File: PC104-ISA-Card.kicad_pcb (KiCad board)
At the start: 2 copper layers, 156.2 x 121.9 mm, 4 parts, among them J1 Bus_PC104_16bit, J2 Bus_ISA_16bit

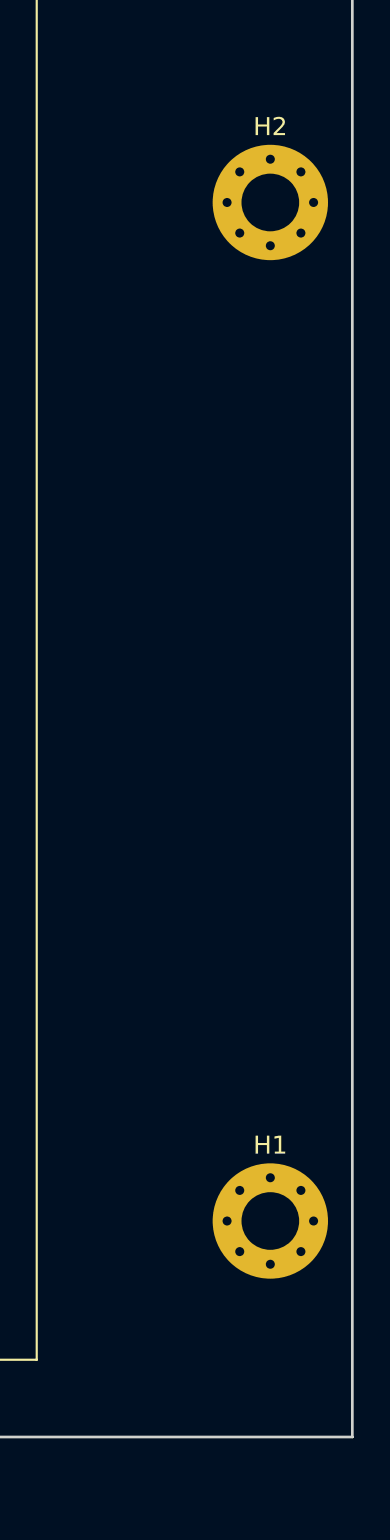
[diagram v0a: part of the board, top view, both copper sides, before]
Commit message: Move mounting holes to correct place for Keystone 9202
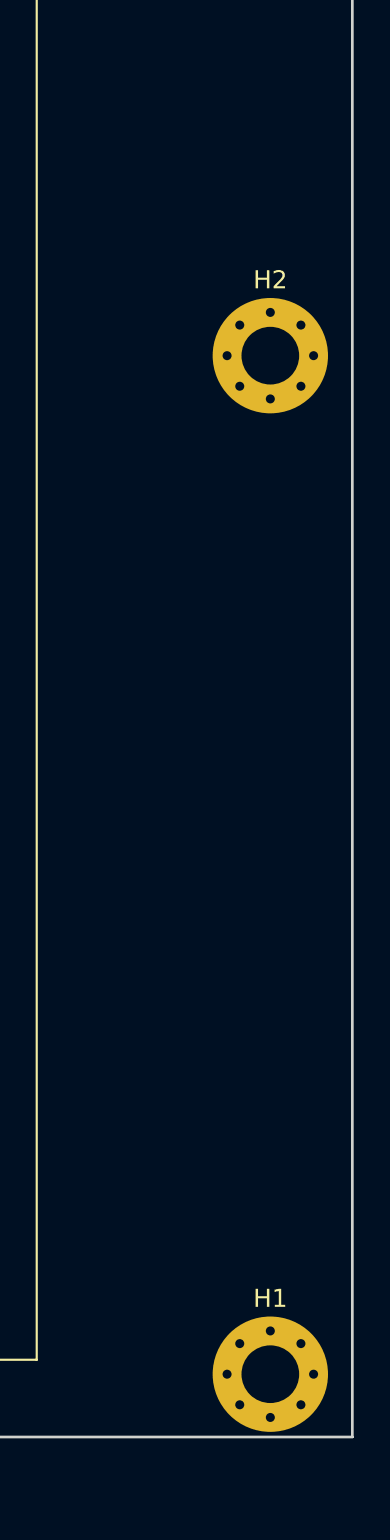
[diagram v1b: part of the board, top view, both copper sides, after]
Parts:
- moved H1 8.50 mm to (195.1, 149.0)
- moved H2 8.50 mm to (195.1, 92.5)
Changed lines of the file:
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@@
   (net 96 "unconnected-(J1-PadC19)")
   (footprint "MountingHole:MountingHole_3.2mm_M3_Pad_Via" (layer "F.Cu")
-    (at 195.08 140.515)
+    (at 195.08 149.015)
     (descr "Mounting Hole 3.2mm, M3")
     (tags "mounting hole 3.2mm m3")
@@
   )
   (footprint "MountingHole:MountingHole_3.2mm_M3_Pad_Via" (layer "F.Cu")
-    (at 195.08 84)
+    (at 195.08 92.5)
     (descr "Mounting Hole 3.2mm, M3")
     (tags "mounting hole 3.2mm m3")

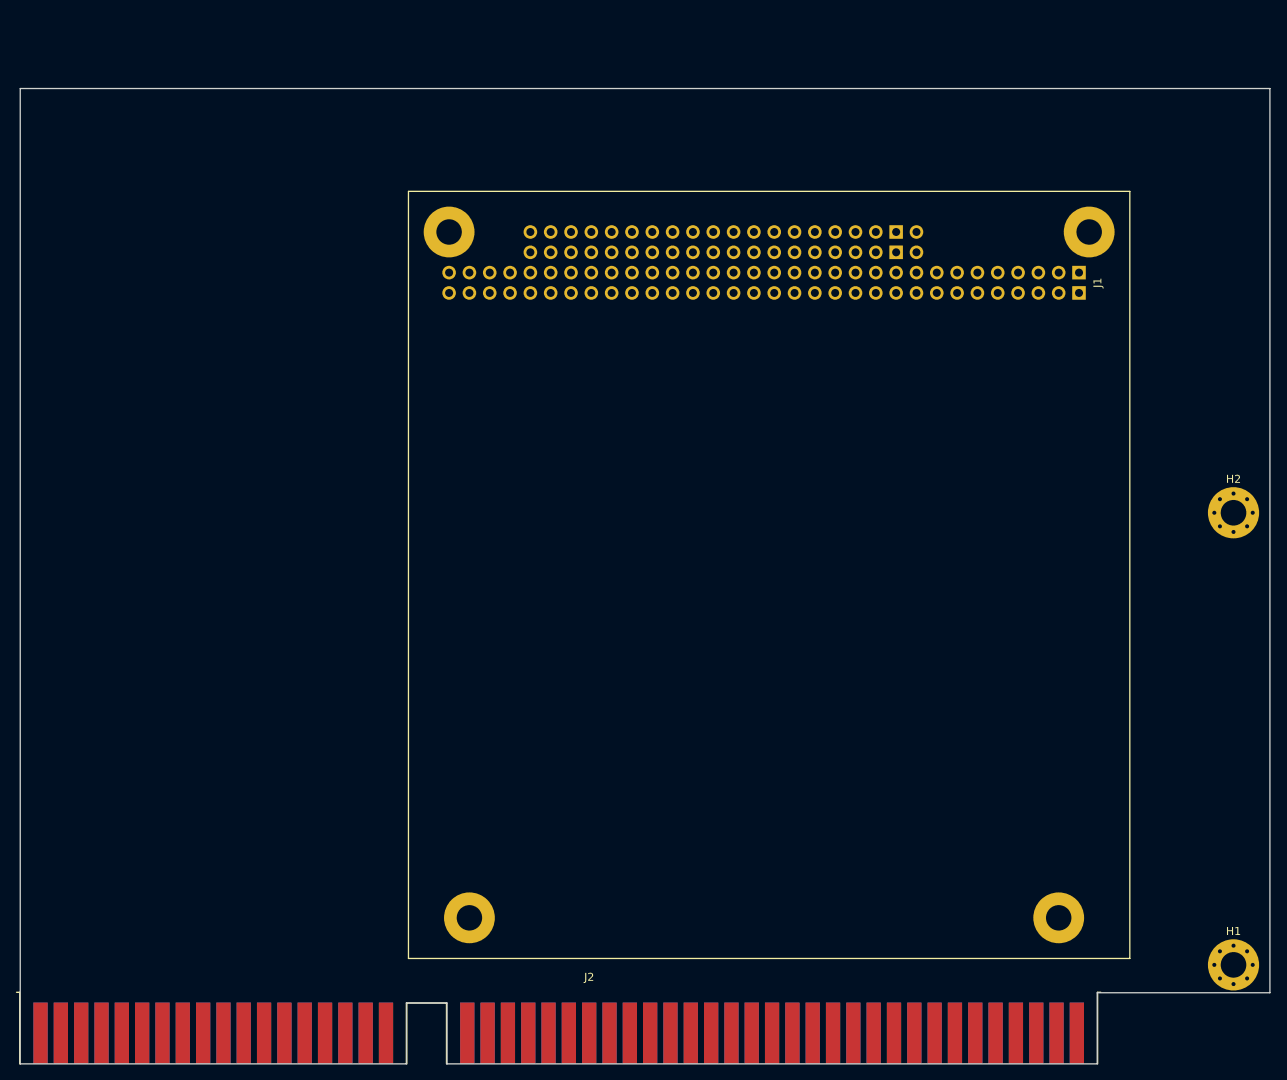
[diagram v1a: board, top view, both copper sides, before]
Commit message: Reduce board height
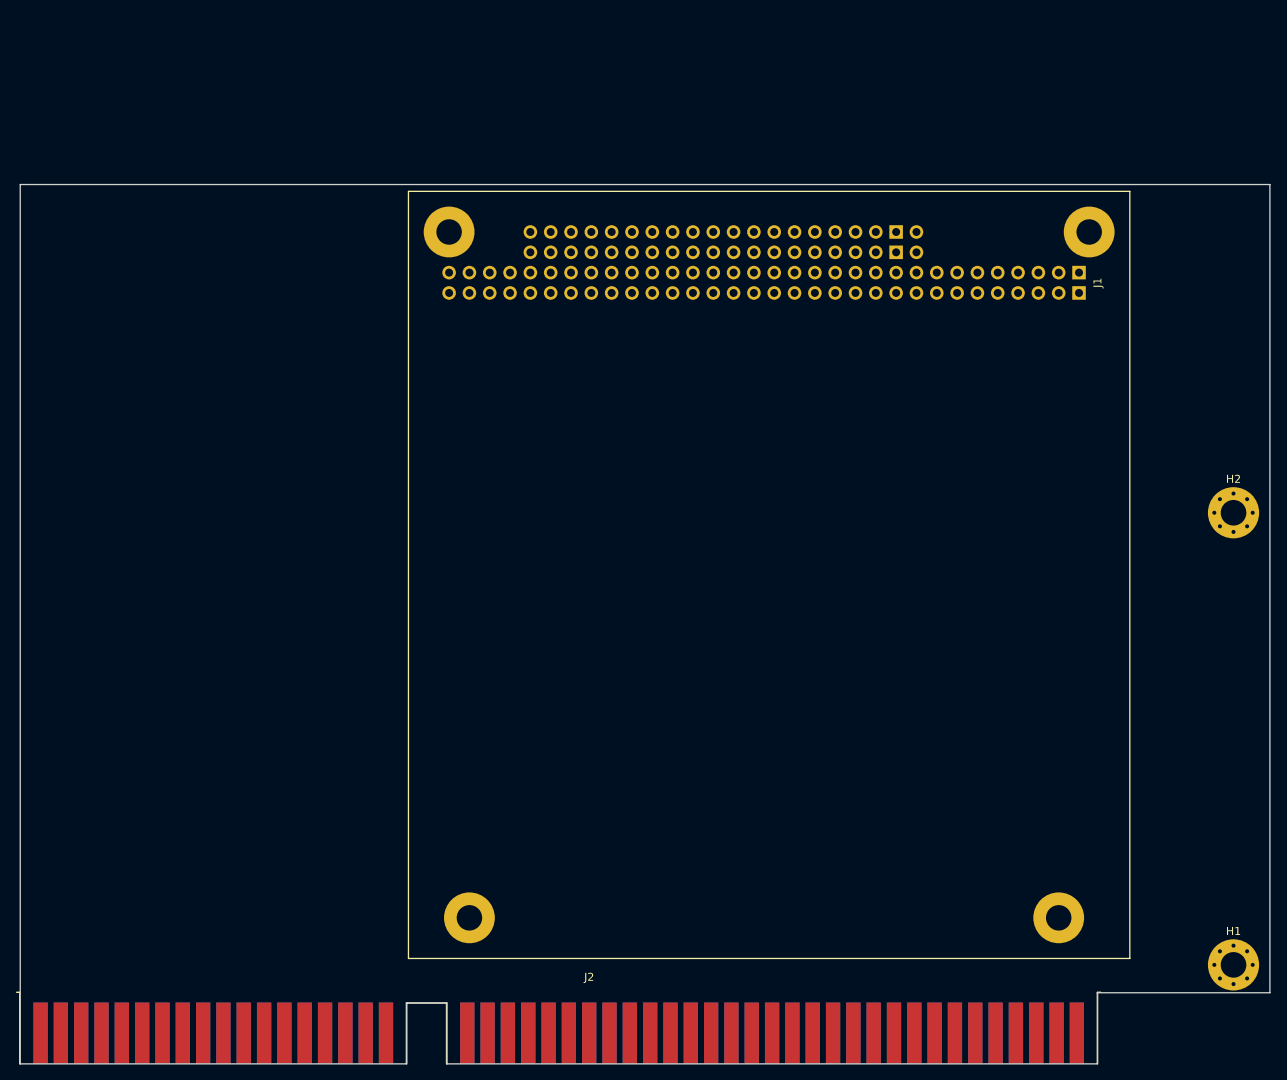
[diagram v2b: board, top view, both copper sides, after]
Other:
- board size 156.2 x 121.9 mm -> 156.2 x 109.9 mm
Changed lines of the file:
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@@
   (gr_line (start 43.42 161.39) (end 91.68 161.39) (layer "Edge.Cuts") (width 0.15))
   (gr_line (start 96.76 161.39) (end 178.04 161.39) (layer "Edge.Cuts") (width 0.15))
-  (gr_line (start 43.42 39.47) (end 43.42 161.39) (layer "Edge.Cuts") (width 0.15))
-  (gr_line (start 199.63 152.5) (end 199.63 39.47) (layer "Edge.Cuts") (width 0.15))
-  (gr_line (start 199.63 39.47) (end 43.42 39.47) (layer "Edge.Cuts") (width 0.15))
+  (gr_line (start 43.42 51.47) (end 43.42 161.39) (layer "Edge.Cuts") (width 0.15))
+  (gr_line (start 199.63 152.5) (end 199.63 51.47) (layer "Edge.Cuts") (width 0.15))
+  (gr_line (start 199.63 51.47) (end 43.42 51.47) (layer "Edge.Cuts") (width 0.15))
   (gr_line (start 96.76 153.77) (end 96.76 161.39) (layer "Edge.Cuts") (width 0.15))
   (gr_line (start 178.04 161.39) (end 178.04 152.5) (layer "Edge.Cuts") (width 0.15))

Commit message: Layout WIP
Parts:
- added C1: 10u, Capacitor_Tantalum_SMD:CP_EIA-7343-15_Kemet-W, F.Cu at (173.0, 71.8)
- added C2: 100n, Capacitor_SMD:C_0603_1608Metric, F.Cu at (65.5, 83.9)
- added C3: 10u, Capacitor_Tantalum_SMD:CP_EIA-7343-15_Kemet-W, F.Cu at (58.7, 91.5)
- added C4: 100n, Capacitor_SMD:C_0603_1608Metric, F.Cu at (61.2, 78.8)
- added C5: 10u, Capacitor_Tantalum_SMD:CP_EIA-7343-15_Kemet-W, F.Cu at (65.4, 101.9)
- added C6: 100n, Capacitor_SMD:C_0603_1608Metric, F.Cu at (70.7, 78.2)
- added C7: 10u, Capacitor_Tantalum_SMD:CP_EIA-7343-15_Kemet-W, F.Cu at (55.5, 101.9)
- added C8: 100n, Capacitor_SMD:C_0603_1608Metric, F.Cu at (71.4, 82.6)
- moved J1 0.28 mm to (181.8, 52.2)
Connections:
- J1 pad A20: /BA1/SA1 -> /BA11/SA11
- J1 pad A30: (no net) -> /BA1/SA1
- J2 pad 8: unconnected-(J2-Pad8) -> /~{SRDY}
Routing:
- net /~{DACK0}: track 0.00 -> 126.5 mm, vias 0 -> 1
- net /~{MEMCS16}: track 0.00 -> 126.5 mm, vias 0 -> 1
- net /~{DACK7}: track 0.00 -> 126.5 mm, vias 0 -> 1
- net /~{DACK6}: track 0.00 -> 126.5 mm, vias 0 -> 1
- net /~{DACK5}: track 0.00 -> 126.5 mm, vias 0 -> 1
- net /IRQ15: track 0.00 -> 126.5 mm, vias 0 -> 1
- net /IRQ14: track 0.00 -> 126.5 mm, vias 0 -> 1
- net /IRQ12: track 0.00 -> 126.5 mm, vias 0 -> 1
- net /IRQ11: track 0.00 -> 126.5 mm, vias 0 -> 1
- net /IRQ10: track 0.00 -> 126.5 mm, vias 0 -> 1
- net /DRQ0: track 0.00 -> 126.5 mm, vias 0 -> 1
- net /~{IOCS16}: track 0.00 -> 126.5 mm, vias 0 -> 1
- net /MASTER/~{MASTER}: track 0.00 -> 126.5 mm, vias 0 -> 1
- net /DRQ7: track 0.00 -> 126.5 mm, vias 0 -> 1
- net /DRQ6: track 0.00 -> 126.5 mm, vias 0 -> 1
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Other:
- copper layers 2 -> 4

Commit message: Added layout
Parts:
- moved C7 138.2 mm to (186.8, 58.7), turned to 180 degrees
- moved C3 130.0 mm to (187.2, 72.4)
- moved C5 126.7 mm to (186.8, 65.5), turned to 180 degrees
- moved C4 126.6 mm to (187.4, 69.1)
- moved C2 126.2 mm to (186.4, 47.9)
- moved C8 118.5 mm to (186.7, 55.4), turned to 180 degrees
- moved C6 117.8 mm to (187.4, 62.2), turned to 180 degrees
- moved C1 24.3 mm to (186.7, 51.8)
- moved J1 21.1 mm to (181.8, 31.2)
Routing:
- net +12V: track 0.00 -> 177.6 mm, vias 0 -> 39
- net -12V: track 0.00 -> 171.8 mm, vias 0 -> 21
- net -5V: track 0.00 -> 142.6 mm, vias 0 -> 7
- net /BA0/SA0: track 0.00 -> 120.9 mm
- net /BA1/SA1: track 0.00 -> 120.2 mm
- net GND: track 126.1 -> 50.5 mm, vias 0 -> 71
- net +5V: track 99.8 -> 61.9 mm, vias 0 -> 25
- net /D15/SD15: track 124.0 -> 149.4 mm
- net /D14/SD14: track 124.0 -> 148.5 mm
- net /DB7/SD7: track 98.3 -> 122.2 mm
- net /D13/SD13: track 124.0 -> 147.7 mm
- net /D12/SD12: track 124.0 -> 147.7 mm
- net /D11/SD11: track 124.0 -> 147.1 mm
- net /D10/SD10: track 124.0 -> 147.0 mm
- net /IRQ2/IRQ9: track 92.6 -> 115.2 mm, vias 0 -> 1
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- added copper zone on In2.Cu, net +12V
- added copper zone on In1.Cu, net +5V
- added copper zone on B.Cu, net GND
- added copper zone on F.Cu, net GND
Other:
- board size 156.2 x 109.9 mm -> 156.2 x 130.9 mm
- board text added: "PC104 ISA Adapter sur5r / manawyrm Rev. A - 2023"

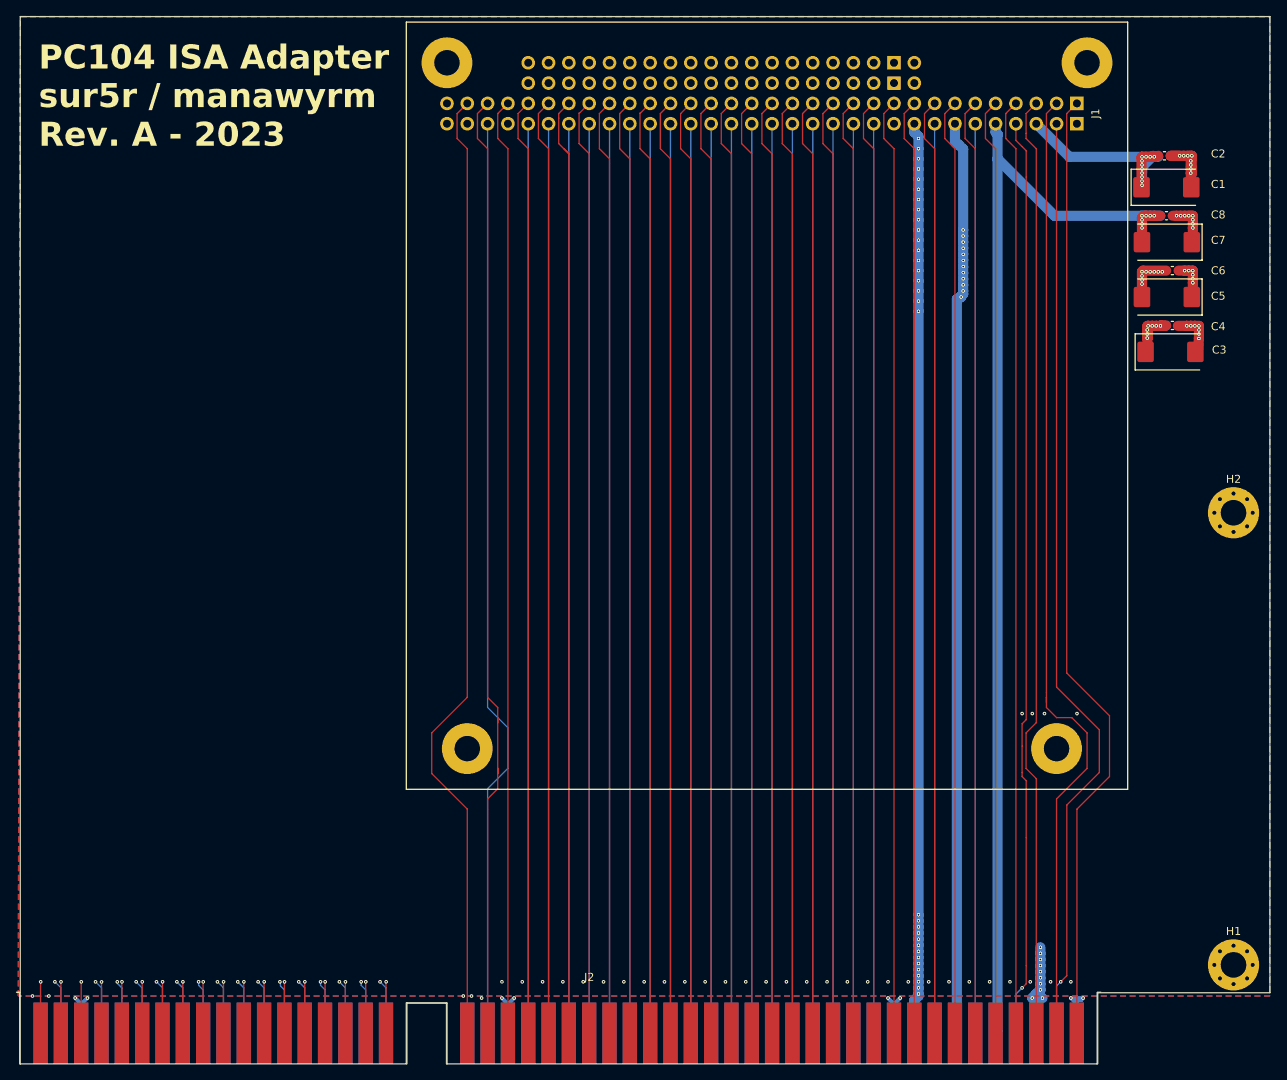
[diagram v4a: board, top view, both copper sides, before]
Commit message: Fix ISA slot grounding
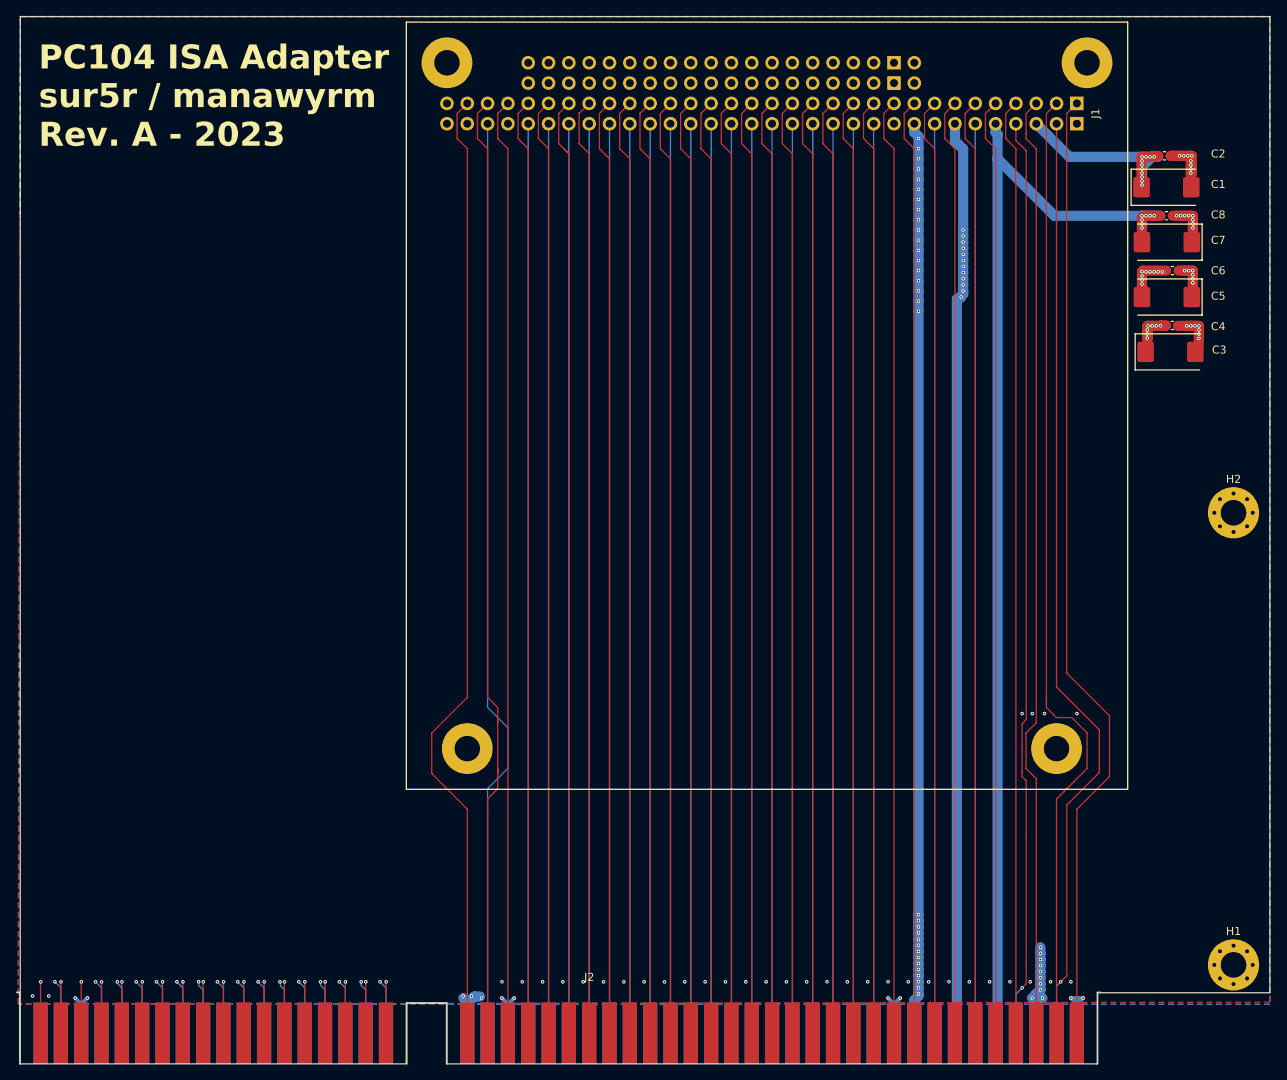
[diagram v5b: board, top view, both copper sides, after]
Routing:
- net GND: track 50.5 -> 60.7 mm
- net -5V: track 142.6 -> 144.2 mm
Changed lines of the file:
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@@
     (pad_to_mask_clearance 0)
     (pad_to_paste_clearance_ratio -0.1)
-    (grid_origin 187.452 45.72)
+    (grid_origin 187.452 0)
     (pcbplotparams
       (layerselection 0x00010fc_ffffffff)
@@
   (via (at 103.632 151.13) (size 0.45) (drill 0.2) (layers "F.Cu" "B.Cu") (free) (net 1))
   (via (at 188.341 47.879) (size 0.45) (drill 0.2) (layers "F.Cu" "B.Cu") (net 1))
+  (segment (start 98.806 153.162) (end 99.3 153.656) (width 1.27) (layer "B.Cu") (net 1))
+  (segment (start 99.3 157.54) (end 99.3 153.856) (width 1.27) (layer "B.Cu") (net 1))
   (segment (start 175.5 157.54) (end 175.5 153.91) (width 0.5) (layer "B.Cu") (net 1))
   (segment (start 175.514 157.526) (end 175.5 157.54) (width 0.5) (layer "B.Cu") (net 1))
+  (segment (start 99.3 153.856) (end 100.188 152.968) (width 1.27) (layer "B.Cu") (net 1))
   (segment (start 152.64 153.938) (end 153.416 153.162) (width 0.5) (layer "B.Cu") (net 1))
   (segment (start 176.276 153.162) (end 176.022 153.416) (width 0.5) (layer "B.Cu") (net 1))
+  (segment (start 99.3 153.656) (end 99.3 157.54) (width 1.27) (layer "B.Cu") (net 1))
   (segment (start 152.64 157.54) (end 152.64 153.938) (width 0.5) (layer "B.Cu") (net 1))
   (segment (start 152.64 157.54) (end 152.64 153.91) (width 0.5) (layer "B.Cu") (net 1))
@@
   (segment (start 176.022 153.416) (end 175.514 153.416) (width 0.5) (layer "B.Cu") (net 1))
   (segment (start 152.64 153.91) (end 151.892 153.162) (width 0.5) (layer "B.Cu") (net 1))
+  (segment (start 100.188 152.968) (end 100.898 152.968) (width 1.27) (layer "B.Cu") (net 1))
   (segment (start 175.5 153.91) (end 174.752 153.162) (width 0.5) (layer "B.Cu") (net 1))
   (segment (start 184.658 48.006) (end 185.166 48.006) (width 1.27) (layer "F.Cu") (net 2))
@@
   (via (at 183.642 56.896) (size 0.45) (drill 0.2) (layers "F.Cu" "B.Cu") (net 35))
   (via (at 183.642 55.88) (size 0.45) (drill 0.2) (layers "F.Cu" "B.Cu") (net 35))
+  (segment (start 183.642 55.372) (end 183.642 56.896) (width 1.27) (layer "B.Cu") (net 35))
   (segment (start 165.579 48.26) (end 165.579 157.301) (width 1.27) (layer "B.Cu") (net 35))
   (segment (start 172.691 55.372) (end 183.642 55.372) (width 1.27) (layer "B.Cu") (net 35))
@@
         (xy 43.434 30.48)
         (xy 199.644 30.48)
-        (xy 199.644 152.908)
-        (xy 43.18 152.908)
+        (xy 199.644 153.67)
+        (xy 43.18 153.924)
       )
     )
@@
         (xy 43.434 30.48)
         (xy 199.644 30.48)
-        (xy 199.644 152.908)
-        (xy 43.18 152.908)
+        (xy 199.644 153.67)
+        (xy 43.18 153.67)
       )
     )
@@
         (xy 43.434 30.48)
         (xy 199.644 30.48)
-        (xy 199.644 152.908)
-        (xy 43.18 152.908)
+        (xy 199.644 153.67)
+        (xy 43.18 153.67)
       )
     )
@@
         (xy 43.434 30.48)
         (xy 199.644 30.48)
-        (xy 199.644 152.908)
-        (xy 43.18 152.908)
+        (xy 199.644 153.924)
+        (xy 43.18 153.924)
       )
     )
